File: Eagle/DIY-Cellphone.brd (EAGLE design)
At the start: 87 x 44.5 mm, 43 parts, among them IC1 MEGA1284, J1 ISP, U1 MCP73831, U7 M10_HDWITHOUT_EXCLUSION, X1 BU-SMA-V, X3 CCM03-3002 R102

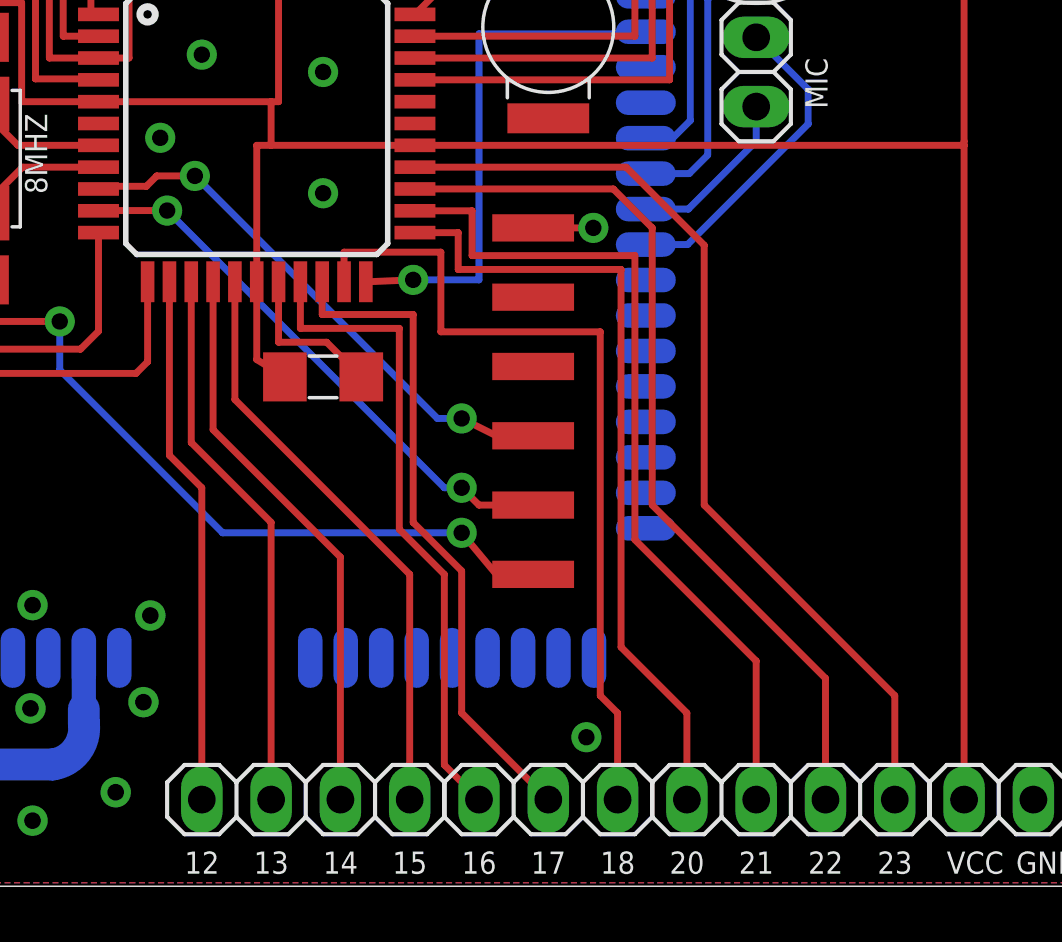
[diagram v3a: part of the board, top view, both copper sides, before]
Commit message: Move FTDI header to edge of board.
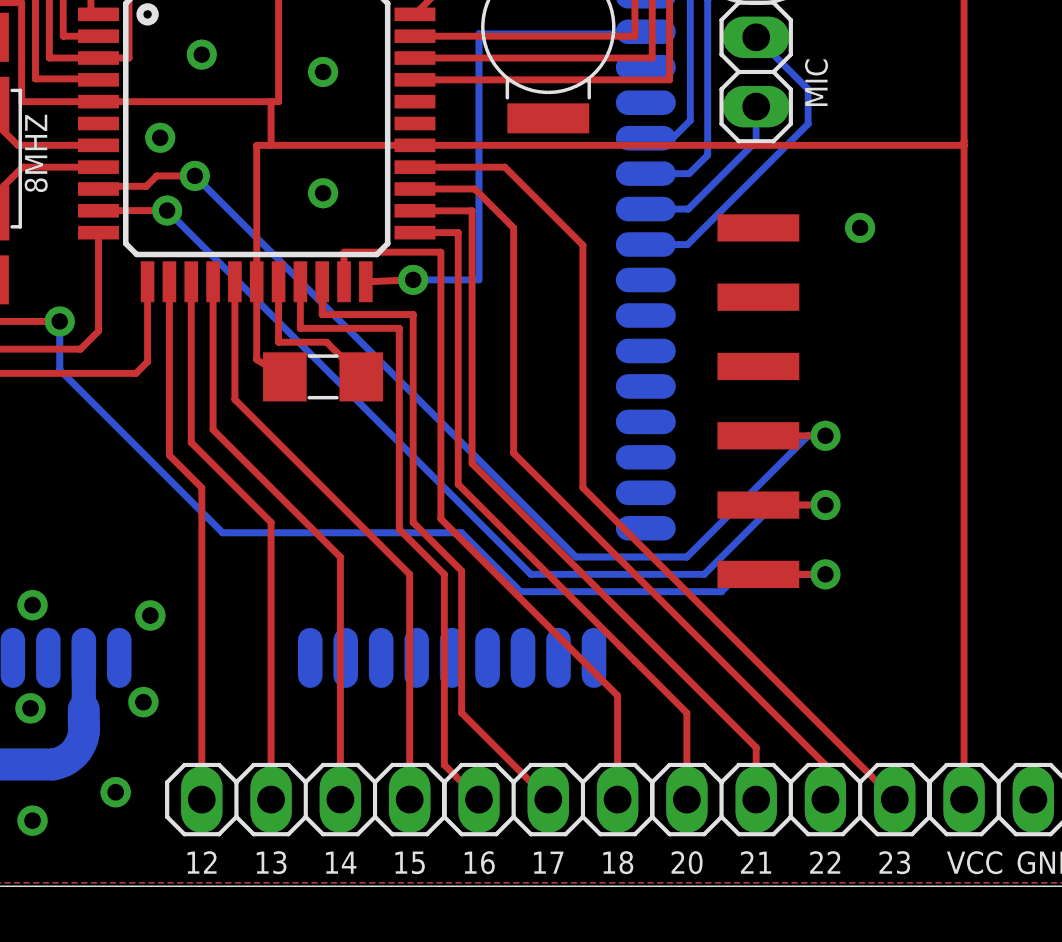
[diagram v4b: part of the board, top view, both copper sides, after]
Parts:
- moved JP7 8.25 mm to (79.4, 17.8)
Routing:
- net RXD0: track 20.0 -> 36.9 mm
- net TXD0: track 20.4 -> 35.7 mm
- net N$5: track 43.4 -> 57.0 mm
- net PC5: track 31.5 -> 28.0 mm
- net PC4: track 29.3 -> 25.8 mm
- net PC2: track 30.8 -> 27.4 mm
- net PC6: track 32.9 -> 29.9 mm
- net PC7: track 35.0 -> 32.4 mm
- net GND: track 88.0 -> 85.8 mm, vias 40 -> 39
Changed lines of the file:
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@@
 <text x="62.23" y="43.18" size="0.8128" layer="26" font="fixed" rot="MR0">31</text>
 <rectangle x1="34.671" y1="12.954" x2="40.259" y2="18.923" layer="42"/>
-<text x="73.66" y="25.4" size="0.8128" layer="27" font="fixed" rot="R90">B</text>
-<text x="73.66" y="9.525" size="0.8128" layer="27" font="fixed" rot="R90">G</text>
+<text x="80.645" y="26.035" size="0.8128" layer="27" font="fixed" rot="R90">B</text>
+<text x="80.645" y="8.89" size="0.8128" layer="27" font="fixed" rot="R90">G</text>
 <text x="63.5" y="1.27" size="0.8128" layer="25" font="fixed" align="top-left">16</text>
 <text x="66.04" y="1.27" size="0.8128" layer="25" font="fixed" align="top-left">17</text>
@@
 <attribute name="VALUE" x="70.485" y="0" size="1.27" layer="27"/>
 </element>
-<element name="JP7" library="cellphone" package="1X06-SMD-NOHOLES" value="" x="71.12" y="17.78" rot="R90"/>
+<element name="JP7" library="cellphone" package="1X06-SMD-NOHOLES" value="" x="79.375" y="17.78" rot="R90"/>
 <element name="JP4" library="pinhead" package="1X03" value="" x="66.675" y="3.175" smashed="yes">
 <attribute name="VALUE" x="62.865" y="0" size="1.27" layer="27"/>
@@
 <wire x1="42.672" y1="22.225" x2="43.304" y2="22.225" width="0.254" layer="1"/>
 <via x="43.561" y="26.67" extent="1-16" drill="0.6"/>
-<via x="68.072" y="5.461" extent="1-16" drill="0.6"/>
-<wire x1="66.12" y1="24.13" x2="68.326" y2="24.13" width="0.254" layer="1"/>
-<via x="68.326" y="24.13" extent="1-16" drill="0.6"/>
 <contactref element="JP8" pad="2"/>
 <contactref element="JP9" pad="2"/>
+<via x="78.105" y="24.13" extent="1-16" drill="0.6"/>
 </signal>
 <signal name="DISP_DATA">
@@
 <contactref element="C1" pad="1"/>
 <contactref element="JP7" pad="1"/>
-<wire x1="66.12" y1="11.43" x2="64.77" y2="11.43" width="0.254" layer="1"/>
-<wire x1="64.77" y1="11.43" x2="63.5" y2="12.954" width="0.254" layer="1"/>
-<via x="63.5" y="12.954" extent="1-16" drill="0.6"/>
 <wire x1="63.5" y1="12.954" x2="54.737" y2="12.954" width="0.254" layer="16"/>
 <wire x1="54.737" y1="12.954" x2="48.768" y2="18.923" width="0.254" layer="16"/>
@@
 <wire x1="41.91" y1="33.401" x2="43.161" y2="33.401" width="0.254" layer="1"/>
 <wire x1="43.161" y1="33.401" x2="43.288" y2="33.636" width="0.254" layer="1"/>
+<wire x1="63.5" y1="12.954" x2="65.659" y2="10.795" width="0.254" layer="16"/>
+<wire x1="65.659" y1="10.795" x2="73.025" y2="10.795" width="0.254" layer="16"/>
+<wire x1="73.025" y1="10.795" x2="73.66" y2="11.43" width="0.254" layer="16"/>
+<wire x1="73.66" y1="11.43" x2="76.835" y2="11.43" width="0.254" layer="16"/>
+<via x="76.835" y="11.43" extent="1-16" drill="0.6"/>
+<wire x1="76.835" y1="11.43" x2="74.375" y2="11.43" width="0.254" layer="1"/>
 </signal>
 <signal name="RXD0">
 <contactref element="IC1" pad="9"/>
 <contactref element="JP7" pad="3"/>
-<wire x1="66.12" y1="16.51" x2="64.77" y2="16.51" width="0.254" layer="1"/>
-<wire x1="64.77" y1="16.51" x2="63.5" y2="17.145" width="0.254" layer="1"/>
-<via x="63.5" y="17.145" extent="1-16" drill="0.6"/>
-<wire x1="63.5" y1="17.145" x2="62.611" y2="17.145" width="0.254" layer="16"/>
-<wire x1="62.611" y1="17.145" x2="53.721" y2="26.035" width="0.254" layer="16"/>
+<wire x1="67.691" y1="12.065" x2="53.721" y2="26.035" width="0.254" layer="16"/>
 <via x="53.721" y="26.035" extent="1-16" drill="0.6"/>
 <wire x1="53.721" y1="26.035" x2="52.324" y2="26.035" width="0.254" layer="1"/>
@@
 <wire x1="51.943" y1="25.654" x2="50.286" y2="25.654" width="0.254" layer="1"/>
 <wire x1="50.286" y1="25.654" x2="50.188" y2="25.556" width="0.254" layer="1"/>
+<wire x1="67.691" y1="12.065" x2="71.755" y2="12.065" width="0.254" layer="16"/>
+<wire x1="71.755" y1="12.065" x2="76.2" y2="16.51" width="0.254" layer="16"/>
+<wire x1="76.2" y1="16.51" x2="76.835" y2="16.51" width="0.254" layer="16"/>
+<via x="76.835" y="16.51" extent="1-16" drill="0.6"/>
+<wire x1="76.835" y1="16.51" x2="74.375" y2="16.51" width="0.254" layer="1"/>
 </signal>
 <signal name="TXD0">
 <contactref element="IC1" pad="10"/>
 <contactref element="JP7" pad="2"/>
-<wire x1="66.12" y1="13.97" x2="64.135" y2="13.97" width="0.254" layer="1"/>
-<wire x1="64.135" y1="13.97" x2="63.5" y2="14.605" width="0.254" layer="1"/>
-<via x="63.5" y="14.605" extent="1-16" drill="0.6"/>
-<wire x1="63.5" y1="14.605" x2="62.865" y2="14.605" width="0.254" layer="16"/>
-<wire x1="62.865" y1="14.605" x2="52.705" y2="24.765" width="0.254" layer="16"/>
+<wire x1="66.04" y1="11.43" x2="52.705" y2="24.765" width="0.254" layer="16"/>
 <via x="52.705" y="24.765" extent="1-16" drill="0.6"/>
 <wire x1="52.705" y1="24.765" x2="50.197" y2="24.765" width="0.254" layer="1"/>
 <wire x1="50.197" y1="24.765" x2="50.188" y2="24.756" width="0.254" layer="1"/>
+<wire x1="66.04" y1="11.43" x2="72.39" y2="11.43" width="0.254" layer="16"/>
+<wire x1="72.39" y1="11.43" x2="74.93" y2="13.97" width="0.254" layer="16"/>
+<wire x1="74.93" y1="13.97" x2="76.835" y2="13.97" width="0.254" layer="16"/>
+<via x="76.835" y="13.97" extent="1-16" drill="0.6"/>
+<wire x1="76.835" y1="13.97" x2="74.375" y2="13.97" width="0.254" layer="1"/>
 </signal>
 <signal name="RXD1">
@@
 <contactref element="IC1" pad="26"/>
 <contactref element="JP1" pad="4"/>
-<wire x1="61.788" y1="26.356" x2="69.529" y2="26.356" width="0.254" layer="1"/>
-<wire x1="69.529" y1="26.356" x2="72.39" y2="23.495" width="0.254" layer="1"/>
-<wire x1="72.39" y1="23.495" x2="72.39" y2="13.97" width="0.254" layer="1"/>
-<wire x1="72.39" y1="13.97" x2="79.375" y2="6.985" width="0.254" layer="1"/>
-<wire x1="79.375" y1="6.985" x2="79.375" y2="3.175" width="0.254" layer="1"/>
+<wire x1="61.788" y1="26.356" x2="65.084" y2="26.356" width="0.254" layer="1"/>
+<wire x1="65.084" y1="26.356" x2="67.945" y2="23.495" width="0.254" layer="1"/>
+<wire x1="67.945" y1="23.495" x2="67.945" y2="14.605" width="0.254" layer="1"/>
+<wire x1="67.945" y1="14.605" x2="79.375" y2="3.175" width="0.254" layer="1"/>
 </signal>
 <signal name="PA4">
@@
 <contactref element="IC1" pad="25"/>
 <contactref element="JP1" pad="3"/>
-<wire x1="61.788" y1="25.556" x2="69.059" y2="25.556" width="0.254" layer="1"/>
-<wire x1="69.059" y1="25.556" x2="70.485" y2="24.13" width="0.254" layer="1"/>
-<wire x1="70.485" y1="24.13" x2="70.485" y2="13.97" width="0.254" layer="1"/>
-<wire x1="70.485" y1="13.97" x2="76.835" y2="7.62" width="0.254" layer="1"/>
-<wire x1="76.835" y1="7.62" x2="76.835" y2="3.175" width="0.254" layer="1"/>
+<wire x1="61.788" y1="25.556" x2="63.979" y2="25.556" width="0.254" layer="1"/>
+<wire x1="63.979" y1="25.556" x2="65.405" y2="24.13" width="0.254" layer="1"/>
+<wire x1="65.405" y1="24.13" x2="65.405" y2="15.875" width="0.254" layer="1"/>
+<wire x1="65.405" y1="15.875" x2="76.835" y2="4.445" width="0.254" layer="1"/>
+<wire x1="76.835" y1="4.445" x2="76.835" y2="3.175" width="0.254" layer="1"/>
 </signal>
 <signal name="PC5">
@@
 <contactref element="JP1" pad="2"/>
 <wire x1="61.788" y1="24.756" x2="63.881" y2="24.756" width="0.254" layer="1"/>
-<wire x1="63.881" y1="24.756" x2="63.881" y2="23.114" width="0.254" layer="1"/>
-<wire x1="63.881" y1="23.114" x2="69.85" y2="23.114" width="0.254" layer="1"/>
-<wire x1="69.85" y1="23.114" x2="69.85" y2="12.7" width="0.254" layer="1"/>
-<wire x1="69.85" y1="12.7" x2="74.295" y2="8.255" width="0.254" layer="1"/>
-<wire x1="74.295" y1="8.255" x2="74.295" y2="3.175" width="0.254" layer="1"/>
+<wire x1="74.295" y1="5.08" x2="74.295" y2="3.175" width="0.254" layer="1"/>
+<wire x1="63.881" y1="24.756" x2="63.881" y2="15.494" width="0.254" layer="1"/>
+<wire x1="63.881" y1="15.494" x2="74.295" y2="5.08" width="0.254" layer="1"/>
 </signal>
 <signal name="PC4">
@@
 <contactref element="JP1" pad="1"/>
 <wire x1="61.788" y1="23.956" x2="63.373" y2="23.956" width="0.254" layer="1"/>
-<wire x1="63.373" y1="23.956" x2="63.373" y2="22.606" width="0.254" layer="1"/>
-<wire x1="63.373" y1="22.606" x2="69.342" y2="22.606" width="0.254" layer="1"/>
-<wire x1="69.342" y1="22.606" x2="69.342" y2="8.763" width="0.254" layer="1"/>
-<wire x1="69.342" y1="8.763" x2="71.755" y2="6.35" width="0.254" layer="1"/>
+<wire x1="69.342" y1="8.763" x2="69.85" y2="8.255" width="0.254" layer="1"/>
+<wire x1="69.85" y1="8.255" x2="71.755" y2="6.35" width="0.254" layer="1"/>
 <wire x1="71.755" y1="6.35" x2="71.755" y2="3.175" width="0.254" layer="1"/>
+<wire x1="63.373" y1="23.956" x2="63.373" y2="14.732" width="0.254" layer="1"/>
+<wire x1="63.373" y1="14.732" x2="69.342" y2="8.763" width="0.254" layer="1"/>
 </signal>
 <signal name="FTDI_VCC">
@@
 <wire x1="59.188" y1="22.156" x2="59.188" y2="23.241" width="0.254" layer="1"/>
 <wire x1="59.188" y1="23.241" x2="62.738" y2="23.241" width="0.254" layer="1"/>
-<wire x1="62.738" y1="23.241" x2="62.738" y2="20.32" width="0.254" layer="1"/>
-<wire x1="62.738" y1="20.32" x2="68.58" y2="20.32" width="0.254" layer="1"/>
-<wire x1="68.58" y1="20.32" x2="68.58" y2="6.985" width="0.254" layer="1"/>
-<wire x1="68.58" y1="6.985" x2="69.215" y2="6.35" width="0.254" layer="1"/>
-<wire x1="69.215" y1="6.35" x2="69.215" y2="3.175" width="0.254" layer="1"/>
+<wire x1="62.738" y1="23.241" x2="62.738" y2="13.462" width="0.254" layer="1"/>
+<wire x1="62.738" y1="13.462" x2="69.215" y2="6.985" width="0.254" layer="1"/>
+<wire x1="69.215" y1="6.985" x2="69.215" y2="3.175" width="0.254" layer="1"/>
 </signal>
 </signals>

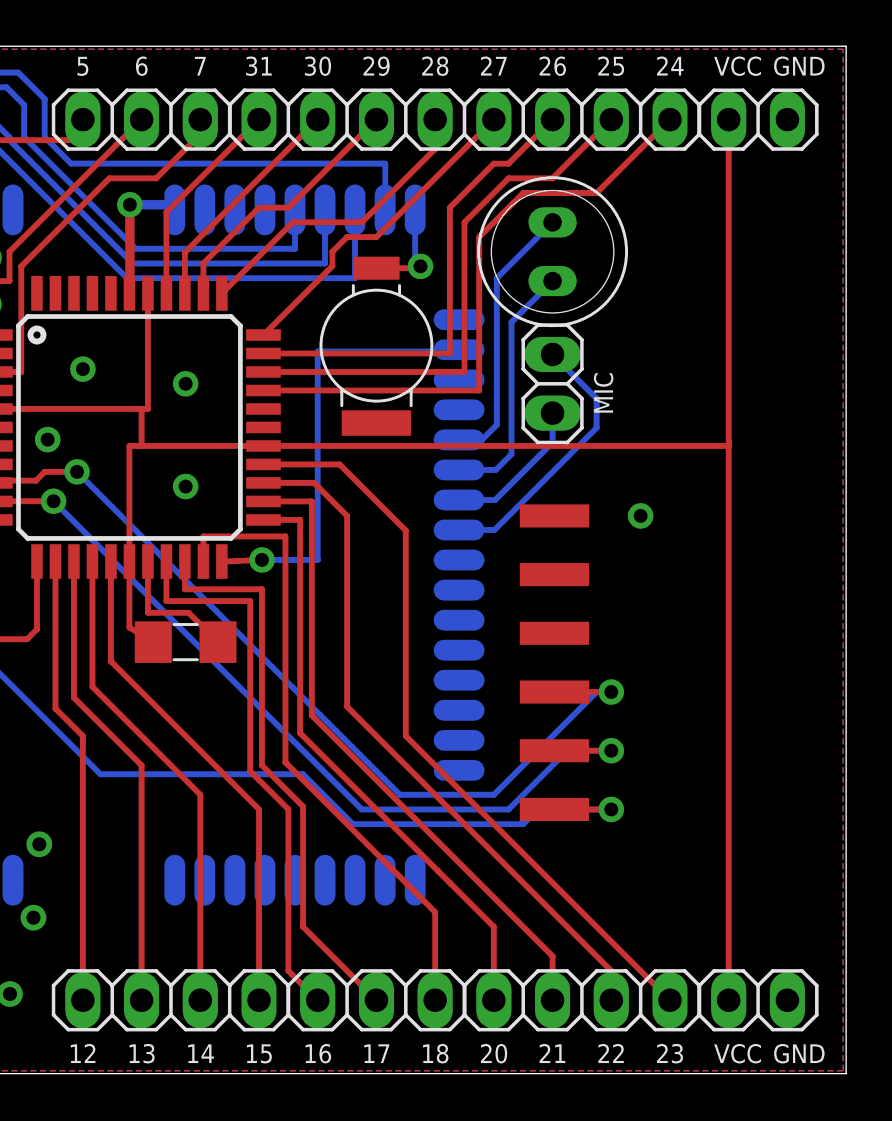
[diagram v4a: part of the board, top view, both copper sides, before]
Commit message: Add LEDs for power and pin 13.
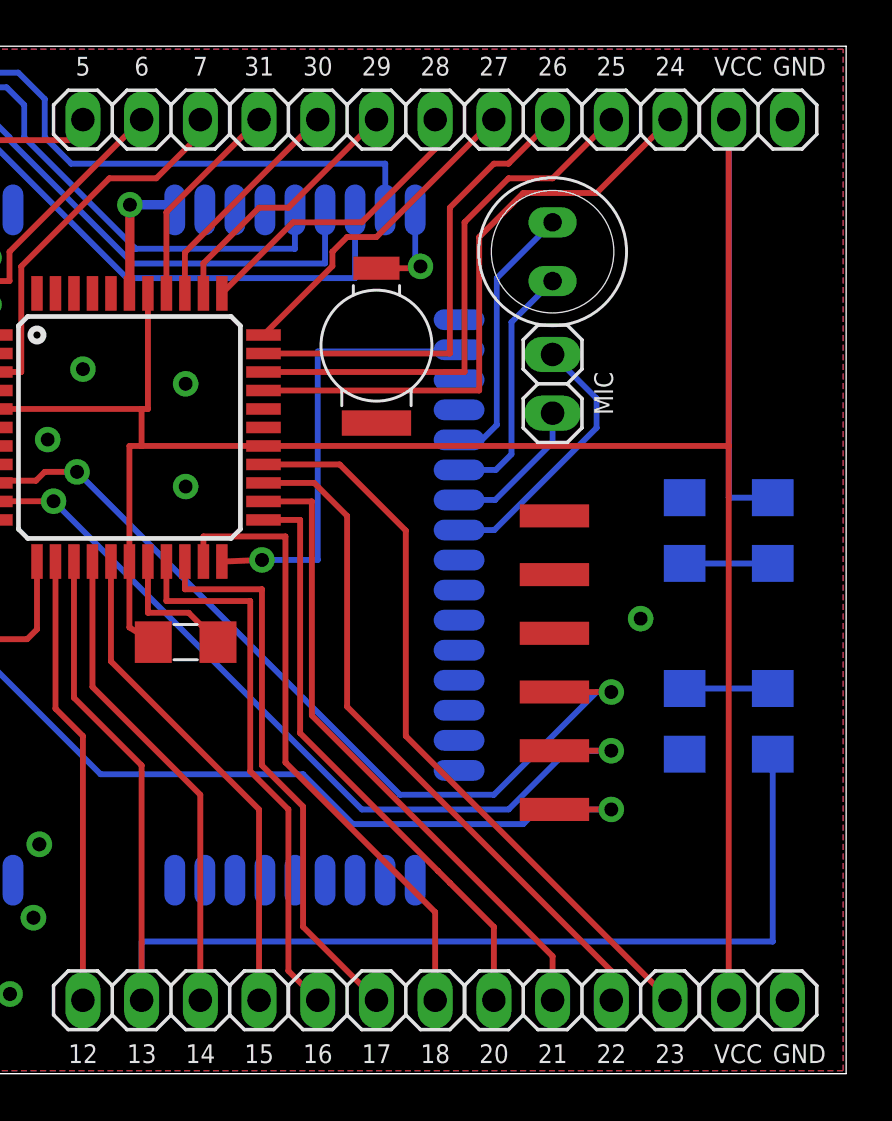
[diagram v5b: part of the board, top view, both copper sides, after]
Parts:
- added LED3: PWR, cellphone-led:1206
- added LED4: 13, cellphone-led:1206
- added R1, R5: 470, cellphone-rcl:R1206
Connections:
- new net N$2: LED3.C, R1.2
- new net N$3: LED4.C, R5.2
- net GND: now also R1.1, R5.1
- net PD5: now also LED4.A
- net VCC: now also LED3.A
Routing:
- net PD5: track 20.2 -> 58.1 mm
- net VCC: track 187.0 -> 205.2 mm
- net N$3: track 0.00 -> 3.81 mm
- net N$2: track 0.00 -> 3.81 mm
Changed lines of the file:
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@@
 <attribute name="VALUE" x="80.645" y="38.1" size="1.27" layer="27"/>
+</element>
+<element name="LED3" library="cellphone-led" package="1206" value="PWR" x="83.82" y="23.495" smashed="yes" rot="MR270">
+<attribute name="VALUE" x="85.725" y="23.495" size="0.8128" layer="28" rot="MR270"/>
+</element>
+<element name="R1" library="cellphone-rcl" package="R1206" value="470" x="80.01" y="23.495" smashed="yes" rot="MR270">
+<attribute name="VALUE" x="78.74" y="23.495" size="0.8128" layer="28" rot="MR270"/>
+</element>
+<element name="LED4" library="cellphone-led" package="1206" value="13" x="83.82" y="15.24" smashed="yes" rot="MR90">
+<attribute name="VALUE" x="85.725" y="15.24" size="0.8128" layer="28" rot="MR270"/>
+</element>
+<element name="R5" library="cellphone-rcl" package="R1206" value="470" x="80.01" y="15.24" smashed="yes" rot="MR90">
+<attribute name="VALUE" x="78.74" y="15.24" size="0.8128" layer="28" rot="MR270"/>
 </element>
 </elements>
@@
 <contactref element="JP9" pad="1"/>
 <wire x1="61.788" y1="27.156" x2="81.915" y2="27.156" width="0.254" layer="1"/>
-<wire x1="81.915" y1="27.156" x2="81.915" y2="27.305" width="0.254" layer="1"/>
-<wire x1="81.915" y1="27.305" x2="81.915" y2="41.275" width="0.254" layer="1"/>
+<wire x1="81.915" y1="27.156" x2="81.915" y2="41.275" width="0.254" layer="1"/>
 <wire x1="81.915" y1="3.175" x2="81.915" y2="27.156" width="0.254" layer="1"/>
+<contactref element="LED3" pad="A"/>
+<wire x1="83.82" y1="24.917" x2="81.915" y2="24.917" width="0.254" layer="16"/>
+<wire x1="81.915" y1="24.917" x2="81.915" y2="41.275" width="0.254" layer="16"/>
 </signal>
 <signal name="ANT" class="4">
@@
 <contactref element="JP8" pad="2"/>
 <contactref element="JP9" pad="2"/>
-<via x="78.105" y="24.13" extent="1-16" drill="0.6"/>
+<via x="78.105" y="19.685" extent="1-16" drill="0.6"/>
+<contactref element="R1" pad="1"/>
+<contactref element="R5" pad="1"/>
 </signal>
 <signal name="DISP_DATA">
@@
 <wire x1="53.588" y1="16.262" x2="56.515" y2="13.335" width="0.254" layer="1"/>
 <wire x1="56.515" y1="13.335" x2="56.515" y2="3.175" width="0.254" layer="1"/>
+<contactref element="LED4" pad="A"/>
+<wire x1="83.82" y1="13.818" x2="83.82" y2="5.715" width="0.254" layer="16"/>
+<wire x1="83.82" y1="5.715" x2="56.515" y2="5.715" width="0.254" layer="16"/>
+<wire x1="56.515" y1="5.715" x2="56.515" y2="3.175" width="0.254" layer="16"/>
 </signal>
 <signal name="PD6">
@@
 <wire x1="69.215" y1="6.985" x2="69.215" y2="3.175" width="0.254" layer="1"/>
 </signal>
+<signal name="N$2">
+<contactref element="LED3" pad="C"/>
+<contactref element="R1" pad="2"/>
+<wire x1="83.82" y1="22.073" x2="80.01" y2="22.073" width="0.254" layer="16"/>
+</signal>
+<signal name="N$3">
+<contactref element="LED4" pad="C"/>
+<contactref element="R5" pad="2"/>
+<wire x1="83.82" y1="16.662" x2="80.01" y2="16.662" width="0.254" layer="16"/>
+</signal>
 </signals>
